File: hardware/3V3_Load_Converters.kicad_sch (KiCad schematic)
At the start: 73 parts, among them J23 61300311121, J24 61300311121, Q26 SI2302DDS-T1-GE3, Q27 SI2302DDS-T1-GE3, Q28 EPC2016C, Q29 EPC2016C, Q30 EPC2016C, Q31 EPC2016C, U21 INA199C3DCKR, U30 LTC3833EUDC-TRPBF, U31 LTC3833EUDC-TRPBF

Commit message: hardware: starting the pcb project
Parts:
- removed Q26, Q27: SI2302DDS-T1-GE3, footprints:SI2302DDS-T1-GE3, symbol SI2302DDS-T1-GE3:SI2302DDS-T1-GE3
- added Q8, Q9: SI2302DDS-T1-GE3, footprints:SI2302DDS-T1-GE3, symbol SI2302DDS-T1-GE3:SI2302DDS-T1-GE3
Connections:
- net 3V3_A_~{EN}: now also Q9.1 (G)
- net 3V3_B_~{EN}: now also Q8.1 (G)
- net GND: now also Q8.2 (S), Q9.2 (S)
- net at U31.7 (RUN): now also Q8.3 (D)
- net at U30.7 (RUN): now also Q9.3 (D)
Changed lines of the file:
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@@
-    )
-  )
-  (symbol (lib_id "SI2302DDS-T1-GE3:SI2302DDS-T1-GE3") (at 115.57 170.18 0) (unit 1)
-    (in_bom yes) (on_board yes) (dnp no)
-    (property "Reference" "Q27" (at 115.57 172.72 0)
-      (effects (font (size 1.27 1.27)) (justify left))
-    )
-    (property "Value" "SI2302DDS-T1-GE3" (at 100.33 175.26 0)
-      (effects (font (size 1.27 1.27)) (justify left))
-    )
-    (property "Footprint" "footprints:SI2302DDS-T1-GE3" (at 104.14 204.47 0) (show_name)
-      (effects (font (size 1.27 1.27)) (justify left top) hide)
-    )
-    (property "Datasheet" "http://www.vishay.com/docs/63653/si2302dds.pdf" (at 91.186 207.264 0) (show_name)
-      (effects (font (size 1.27 1.27)) (justify left top) hide)
-    )
-    (property "Height" "1.12" (at 127 568.91 0)
-      (effects (font (size 1.27 1.27)) (justify left top) hide)
-    )
-    (property "Mouser Part Number" "78-SI2302DDS-T1-GE3" (at 127 668.91 0)
-      (effects (font (size 1.27 1.27)) (justify left top) hide)
-    )
-    (property "Mouser Price/Stock" "https://www.mouser.co.uk/ProductDetail/Vishay-Semiconductors/SI2302DDS-T1-GE3?qs=MxnWX8BLHKdaCSNWhg%252BxLA%3D%3D" (at 127 768.91 0)
-      (effects (font (size 1.27 1.27)) (justify left top) hide)
-    )
-    (property "Manufacturer_Name" "Vishay" (at 127 868.91 0)
-      (effects (font (size 1.27 1.27)) (justify left top) hide)
-    )
-    (property "Manufacturer_Part_Number" "SI2302DDS-T1-GE3" (at 127 968.91 0)
-      (effects (font (size 1.27 1.27)) (justify left top) hide)
-    )
-    (pin "1")
-    (pin "2")
-    (pin "3")
-    (instances
-      (project "eps-re_project"
-        (path "/2eebaa11-d7ed-4bfd-bc8e-988f68654d29/6f34948c-43a8-4614-b8ed-90c5b6b9b243"
-          (reference "Q27") (unit 1)
-        )
-        (path "/2eebaa11-d7ed-4bfd-bc8e-988f68654d29/6cd5fe02-9b19-49bf-9109-b0a2c2f10c14"
-          (reference "Q2") (unit 1)
-        )
-      )
     )
   )
@@
         (path "/2eebaa11-d7ed-4bfd-bc8e-988f68654d29/6f34948c-43a8-4614-b8ed-90c5b6b9b243"
           (reference "C113") (unit 1)
+        )
+      )
+    )
+  )
+  (symbol (lib_id "SI2302DDS-T1-GE3:SI2302DDS-T1-GE3") (at 115.57 170.18 0) (unit 1)
+    (in_bom yes) (on_board yes) (dnp no)
+    (property "Reference" "Q8" (at 99.06 160.02 0)
+      (effects (font (size 1.27 1.27)) (justify left))
+    )
+    (property "Value" "SI2302DDS-T1-GE3" (at 99.06 162.56 0)
+      (effects (font (size 1.27 1.27)) (justify left))
+    )
+    (property "Footprint" "footprints:SI2302DDS-T1-GE3" (at 104.14 204.47 0)
+      (effects (font (size 1.27 1.27)) (justify left top) hide)
+    )
+    (property "Datasheet" "http://www.vishay.com/docs/63653/si2302dds.pdf" (at 91.186 207.264 0)
+      (effects (font (size 1.27 1.27)) (justify left top) hide)
+    )
+    (property "Height" "1.12" (at 127 568.91 0)
+      (effects (font (size 1.27 1.27)) (justify left top) hide)
+    )
+    (property "Mouser Part Number" "78-SI2302DDS-T1-GE3" (at 127 668.91 0)
+      (effects (font (size 1.27 1.27)) (justify left top) hide)
+    )
+    (property "Mouser Price/Stock" "https://www.mouser.co.uk/ProductDetail/Vishay-Semiconductors/SI2302DDS-T1-GE3?qs=MxnWX8BLHKdaCSNWhg%252BxLA%3D%3D" (at 127 768.91 0)
+      (effects (font (size 1.27 1.27)) (justify left top) hide)
+    )
+    (property "Manufacturer_Name" "Vishay" (at 127 868.91 0)
+      (effects (font (size 1.27 1.27)) (justify left top) hide)
+    )
+    (property "Manufacturer_Part_Number" "SI2302DDS-T1-GE3" (at 127 968.91 0)
+      (effects (font (size 1.27 1.27)) (justify left top) hide)
+    )
+    (pin "1")
+    (pin "2")
+    (pin "3")
+    (instances
+      (project "eps-re_project"
+        (path "/2eebaa11-d7ed-4bfd-bc8e-988f68654d29/6f34948c-43a8-4614-b8ed-90c5b6b9b243"
+          (reference "Q8") (unit 1)
         )
       )
@@
     )
   )
+  (symbol (lib_id "SI2302DDS-T1-GE3:SI2302DDS-T1-GE3") (at 115.57 69.85 0) (unit 1)
+    (in_bom yes) (on_board yes) (dnp no)
+    (property "Reference" "Q9" (at 99.06 59.69 0)
+      (effects (font (size 1.27 1.27)) (justify left))
+    )
+    (property "Value" "SI2302DDS-T1-GE3" (at 99.06 62.23 0)
+      (effects (font (size 1.27 1.27)) (justify left))
+    )
+    (property "Footprint" "footprints:SI2302DDS-T1-GE3" (at 104.14 104.14 0)
+      (effects (font (size 1.27 1.27)) (justify left top) hide)
+    )
+    (property "Datasheet" "http://www.vishay.com/docs/63653/si2302dds.pdf" (at 91.186 106.934 0)
+      (effects (font (size 1.27 1.27)) (justify left top) hide)
+    )
+    (property "Height" "1.12" (at 127 468.58 0)
+      (effects (font (size 1.27 1.27)) (justify left top) hide)
+    )
+    (property "Mouser Part Number" "78-SI2302DDS-T1-GE3" (at 127 568.58 0)
+      (effects (font (size 1.27 1.27)) (justify left top) hide)
+    )
+    (property "Mouser Price/Stock" "https://www.mouser.co.uk/ProductDetail/Vishay-Semiconductors/SI2302DDS-T1-GE3?qs=MxnWX8BLHKdaCSNWhg%252BxLA%3D%3D" (at 127 668.58 0)
+      (effects (font (size 1.27 1.27)) (justify left top) hide)
+    )
+    (property "Manufacturer_Name" "Vishay" (at 127 768.58 0)
+      (effects (font (size 1.27 1.27)) (justify left top) hide)
+    )
+    (property "Manufacturer_Part_Number" "SI2302DDS-T1-GE3" (at 127 868.58 0)
+      (effects (font (size 1.27 1.27)) (justify left top) hide)
+    )
+    (pin "1")
+    (pin "2")
+    (pin "3")
+    (instances
+      (project "eps-re_project"
+        (path "/2eebaa11-d7ed-4bfd-bc8e-988f68654d29/6f34948c-43a8-4614-b8ed-90c5b6b9b243"
+          (reference "Q9") (unit 1)
+        )
+      )
+    )
+  )
   (symbol (lib_id "CRCW0603100KFKEAHP:CRCW0603100KFKEAHP") (at 106.68 82.55 90) (unit 1)
     (in_bom yes) (on_board yes) (dnp no) (fields_autoplaced)
@@
         )
       )
-    )
-  )
-  (symbol (lib_id "SI2302DDS-T1-GE3:SI2302DDS-T1-GE3") (at 115.57 69.85 0) (unit 1)
-    (in_bom yes) (on_board yes) (dnp no)
-    (property "Reference" "Q26" (at 114.808 60.198 0)
-      (effects (font (size 1.27 1.27)) (justify left))
-    )
-    (property "Value" "SI2302DDS-T1-GE3" (at 99.568 62.738 0)
-      (effects (font (size 1.27 1.27)) (justify left))
-    )
-    (property "Footprint" "footprints:SI2302DDS-T1-GE3" (at 104.14 104.14 0) (show_name)
-      (effects (font (size 1.27 1.27)) (justify left top) hide)
-    )
-    (property "Datasheet" "http://www.vishay.com/docs/63653/si2302dds.pdf" (at 91.186 106.934 0) (show_name)
-      (effects (font (size 1.27 1.27)) (justify left top) hide)
-    )
-    (property "Height" "1.12" (at 127 468.58 0)
-      (effects (font (size 1.27 1.27)) (justify left top) hide)
-    )
-    (property "Mouser Part Number" "78-SI2302DDS-T1-GE3" (at 127 568.58 0)
-      (effects (font (size 1.27 1.27)) (justify left top) hide)
-    )
-    (property "Mouser Price/Stock" "https://www.mouser.co.uk/ProductDetail/Vishay-Semiconductors/SI2302DDS-T1-GE3?qs=MxnWX8BLHKdaCSNWhg%252BxLA%3D%3D" (at 127 668.58 0)
-      (effects (font (size 1.27 1.27)) (justify left top) hide)
-    )
-    (property "Manufacturer_Name" "Vishay" (at 127 768.58 0)
-      (effects (font (size 1.27 1.27)) (justify left top) hide)
-    )
-    (property "Manufacturer_Part_Number" "SI2302DDS-T1-GE3" (at 127 868.58 0)
-      (effects (font (size 1.27 1.27)) (justify left top) hide)
-    )
-    (pin "1")
-    (pin "2")
-    (pin "3")
-    (instances
-      (project "eps-re_project"
-        (path "/2eebaa11-d7ed-4bfd-bc8e-988f68654d29/6f34948c-43a8-4614-b8ed-90c5b6b9b243"
-          (reference "Q26") (unit 1)
-        )
-        (path "/2eebaa11-d7ed-4bfd-bc8e-988f68654d29/6cd5fe02-9b19-49bf-9109-b0a2c2f10c14"
-          (reference "Q1") (unit 1)
-        )
-      )

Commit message: hardware: Updating 3D models, component placement and more.
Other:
- title: (none) -> Reliability Enhanced Electrical Power System
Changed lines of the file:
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@@
 (kicad_sch (version 20230121) (generator eeschema)
   (paper "A3")
+  (title_block
+    (title "Reliability Enhanced Electrical Power System")
+    (date "2023-08-03")
+    (rev "v0.0")
+    (comment 1 "João C. E. Barcellos <joaoclaudiobarcellos@gmail.com>")
+    (comment 2 "Laura Debastiani <laudebastiani@gmail.com>")
+  )
   (junction (at 346.71 29.21) (diameter 0) (color 0 0 0 0)
   )

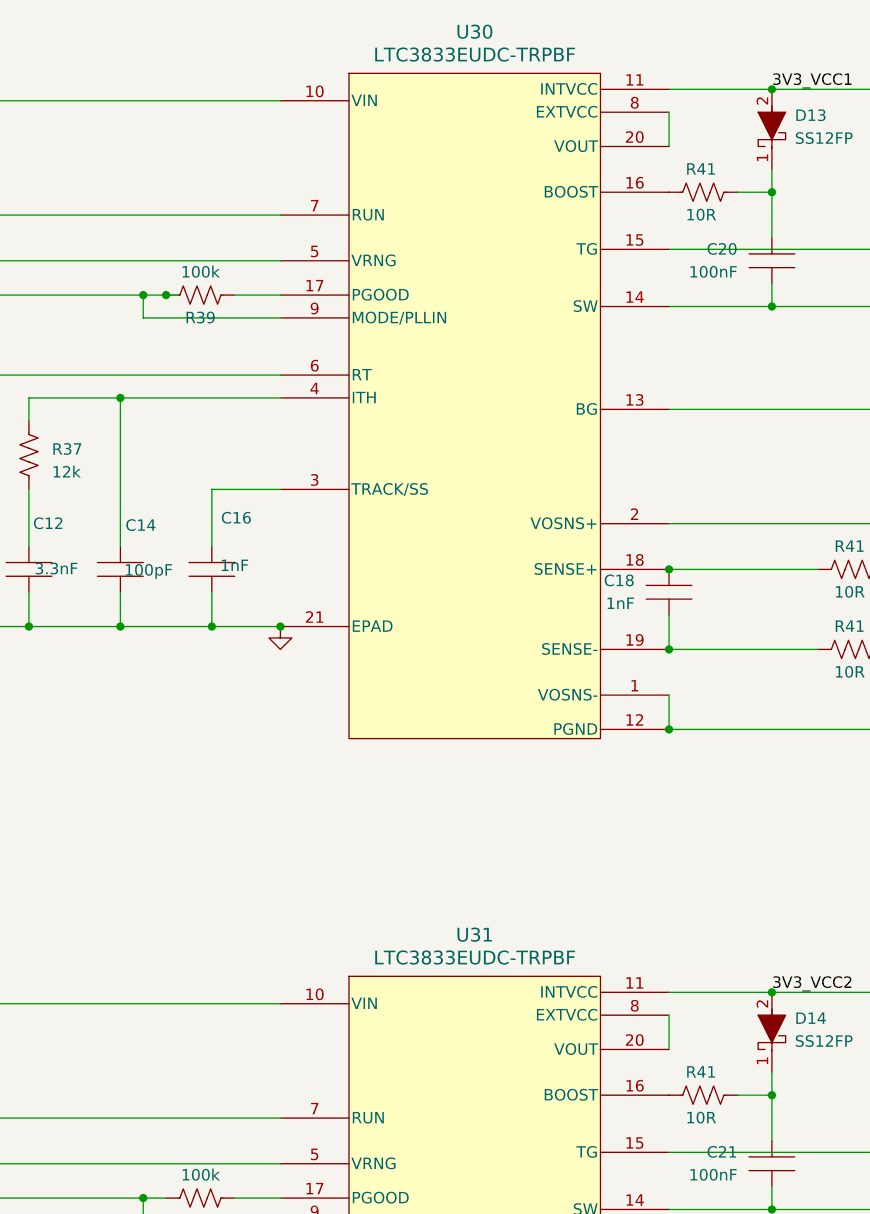
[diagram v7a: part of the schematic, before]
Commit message: hardware: Updating some zones in the layout and making minor changes in the schematic.
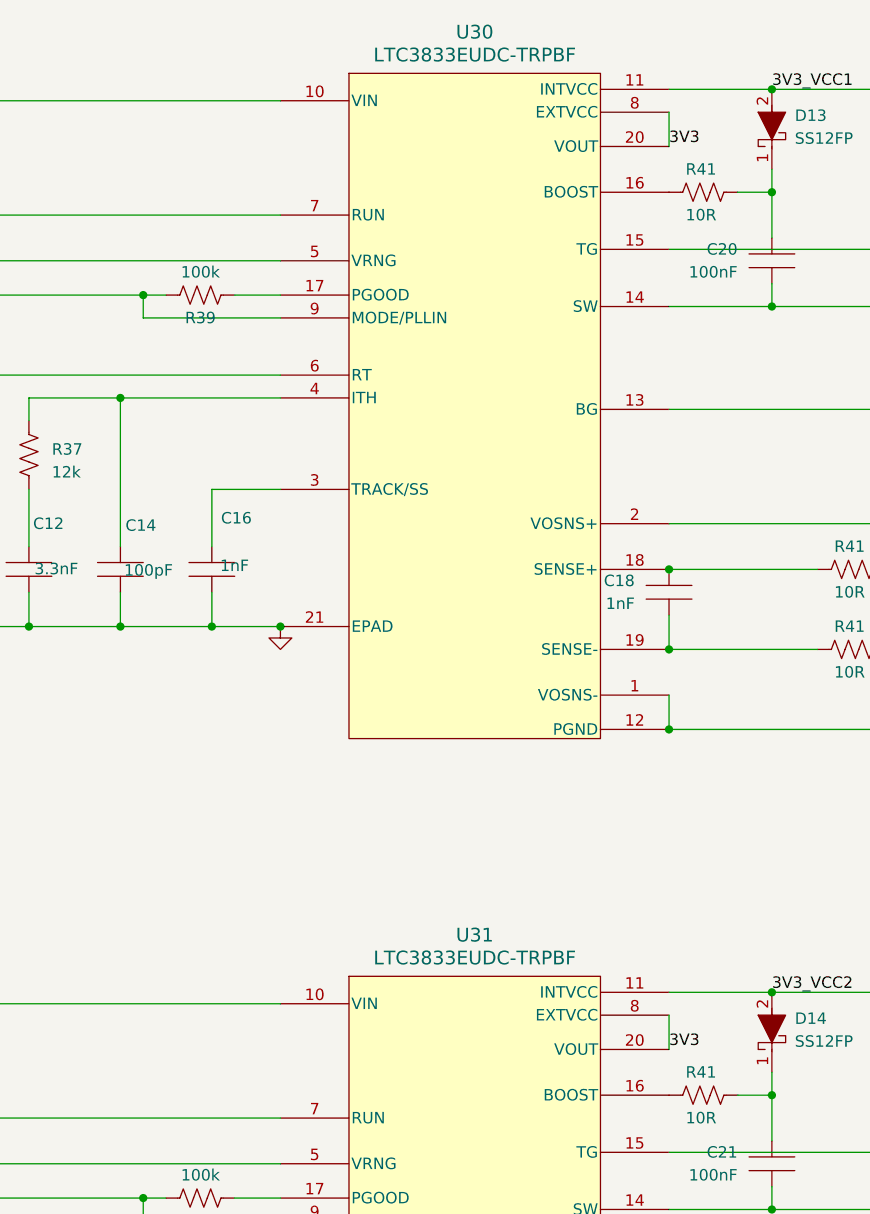
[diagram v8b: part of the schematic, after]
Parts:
- J23, J24: footprint footprints:61300311121 -> footprints:three_position_jumper
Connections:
- net 3V3: now also U30.20 (VOUT), U30.8 (EXTVCC), U31.20 (VOUT), U31.8 (EXTVCC)
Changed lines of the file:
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@@
   (junction (at 173.99 184.15) (diameter 0) (color 0 0 0 0)
   )
-  (junction (at 189.23 46.99) (diameter 0) (color 0 0 0 0)
-  )
   (junction (at 347.98 195.58) (diameter 0) (color 0 0 0 0)
   )
@@
     (stroke (width 0) (type default))
   )
-  (wire (pts (xy 189.23 46.99) (xy 190.5 46.99))
-    (stroke (width 0) (type default))
-  )
   (wire (pts (xy 256.54 146.05) (xy 256.54 148.59))
     (stroke (width 0) (type default))
@@
     (effects (font (size 1.27 1.27)) (justify left bottom))
   )
+  (label "3V3" (at 245.11 130.81 0) (fields_autoplaced)
+    (effects (font (size 1.27 1.27)) (justify left bottom))
+  )
   (label "3V3" (at 383.54 148.59 0) (fields_autoplaced)
     (effects (font (size 1.27 1.27)) (justify left bottom))
   )
+  (label "3V3" (at 245.11 30.48 0) (fields_autoplaced)
+    (effects (font (size 1.27 1.27)) (justify left bottom))
+  )
   (label "3V3_VCC1" (at 134.62 46.99 0) (fields_autoplaced)
     (effects (font (size 1.27 1.27)) (justify left bottom))
@@
       (effects (font (size 1.27 1.27)) (justify left))
     )
-    (property "Footprint" "footprints:61300311121" (at 134.62 86.03 0)
+    (property "Footprint" "footprints:three_position_jumper" (at 134.62 86.03 0)
       (effects (font (size 1.27 1.27)) (justify left top) hide)
     )
@@
       (effects (font (size 1.27 1.27)) (justify left))
     )
-    (property "Footprint" "footprints:61300311121" (at 134.62 186.36 0)
+    (property "Footprint" "footprints:three_position_jumper" (at 134.62 186.36 0)
       (effects (font (size 1.27 1.27)) (justify left top) hide)
     )
